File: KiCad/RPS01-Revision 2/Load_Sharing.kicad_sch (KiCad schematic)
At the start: 11 parts, among them U1 NP100P04PLG-E1-AY, U2 NP100P04PLG-E1-AY, U3 NP100P04PLG-E1-AY, U4 LTC4416EMS-1-TRPBF, U5 NP100P04PLG-E1-AY, U6 NP100P04PLG-E1-AY, U7 NP100P04PLG-E1-AY

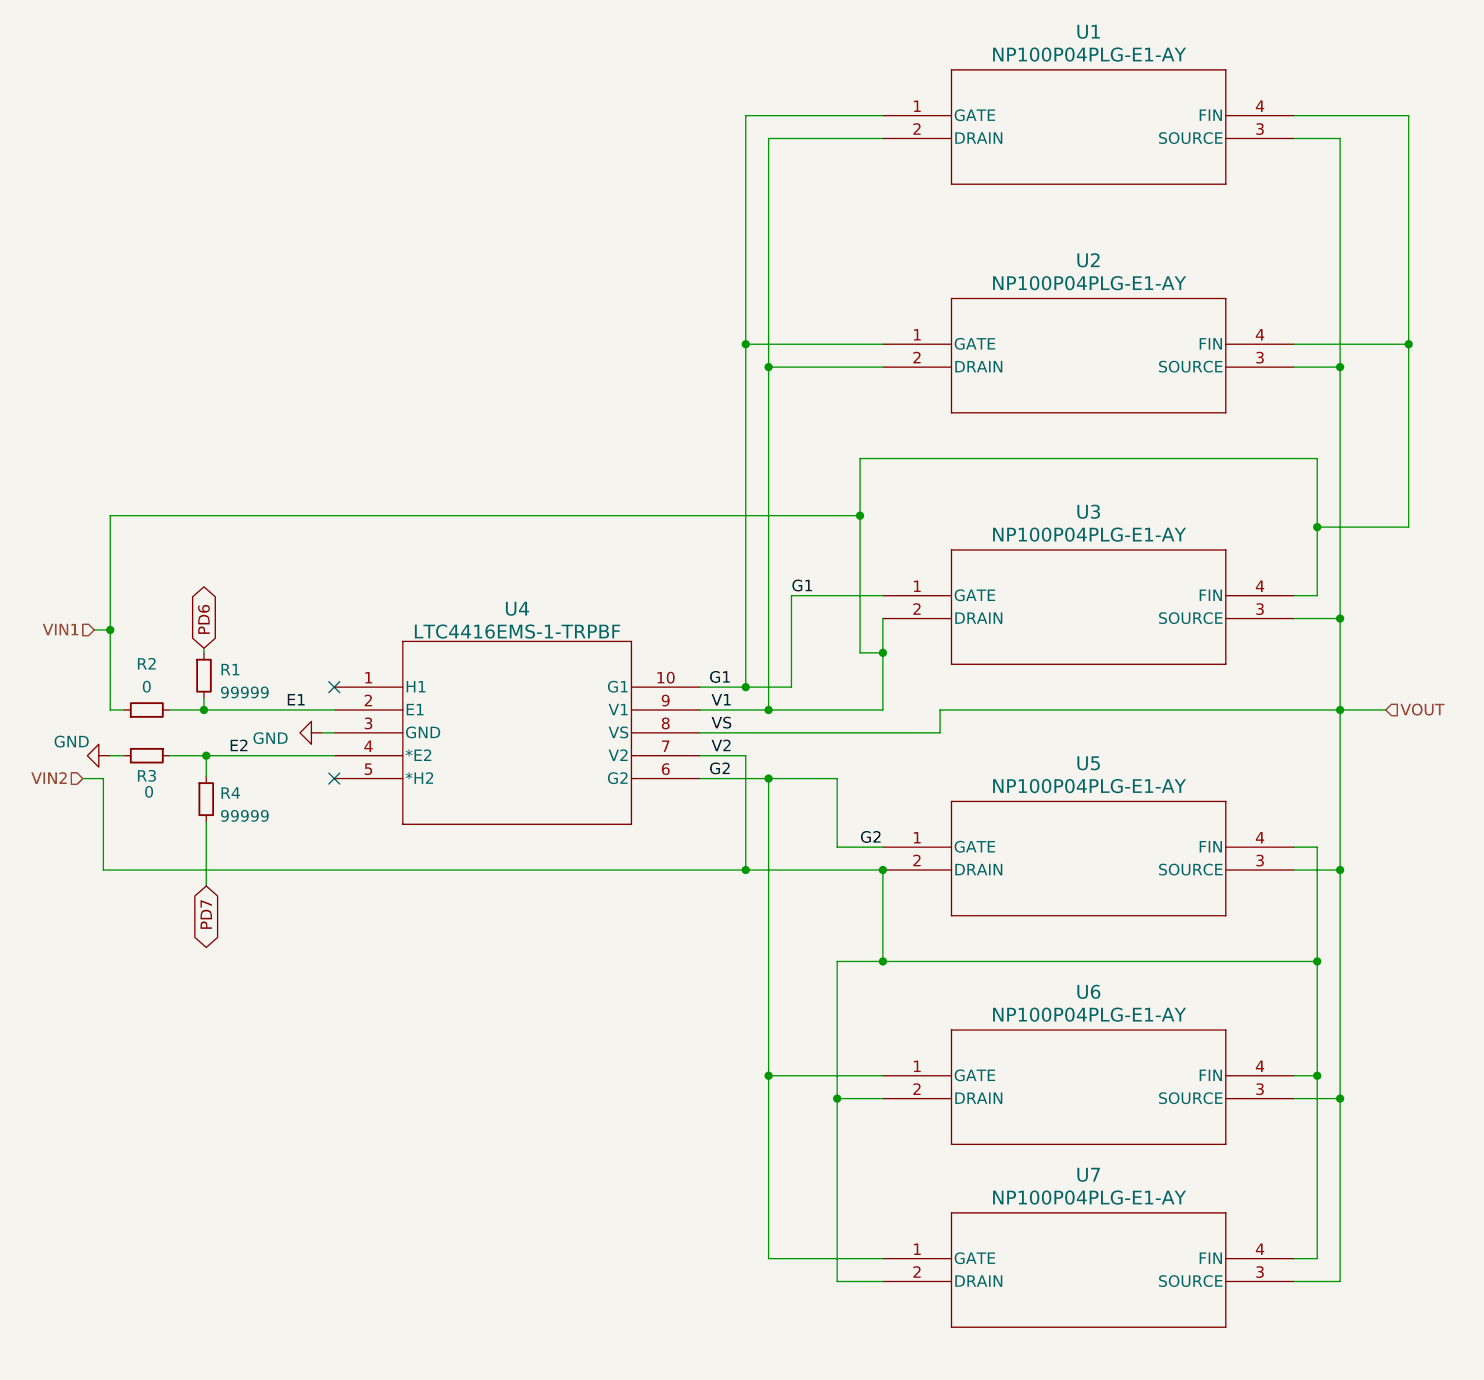
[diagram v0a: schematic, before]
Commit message: Load Sharing
Changed wiring for the reversed MOSFETs
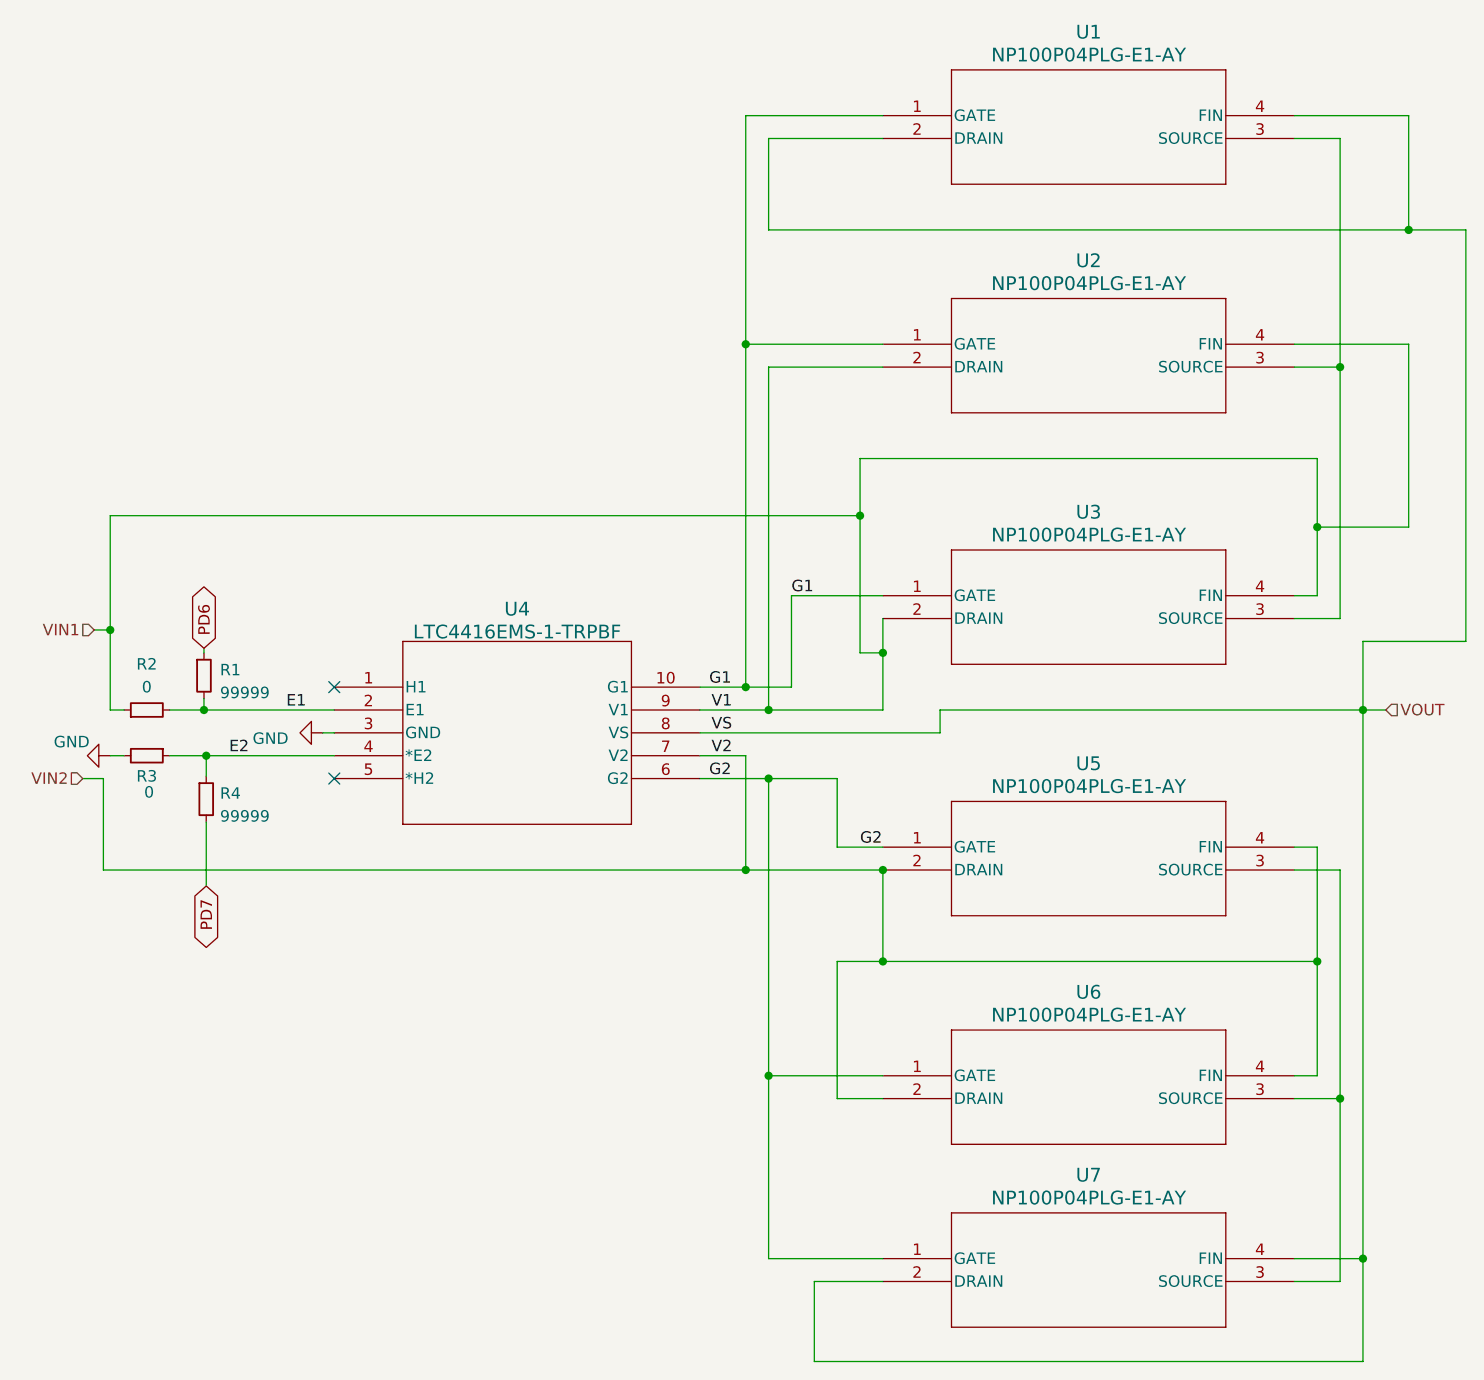
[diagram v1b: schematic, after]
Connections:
- net VIN1: no longer U1.2 (DRAIN), U1.4 (FIN)
- net VIN2: no longer U7.2 (DRAIN), U7.4 (FIN)
- net VOUT: now also U1.2 (DRAIN), U1.4 (FIN), U7.2 (DRAIN), U7.4 (FIN); no longer U1.3 (SOURCE), U2.3 (SOURCE), U3.3 (SOURCE), U5.3 (SOURCE), U6.3 (SOURCE), U7.3 (SOURCE)
- new net: U1.3 (SOURCE), U2.3 (SOURCE), U3.3 (SOURCE)
- new net: U5.3 (SOURCE), U6.3 (SOURCE), U7.3 (SOURCE)
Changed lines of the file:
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@@
 (kicad_sch (version 20230121) (generator eeschema)
   (paper "A4")
-  (junction (at 162.56 104.14) (diameter 0) (color 0 0 0 0)
-  )
-  (junction (at 162.56 93.98) (diameter 0) (color 0 0 0 0)
-  )
-  (junction (at 160.02 144.78) (diameter 0) (color 0 0 0 0)
+  (junction (at 165.1 165.1) (diameter 0) (color 0 0 0 0)
   )
   (junction (at 111.76 121.92) (diameter 0) (color 0 0 0 0)
@@
   (junction (at 162.56 66.04) (diameter 0) (color 0 0 0 0)
   )
-  (junction (at 162.56 121.92) (diameter 0) (color 0 0 0 0)
-  )
   (junction (at 36.576 109.22) (diameter 0) (color 0 0 0 0)
   )
@@
   (junction (at 96.52 121.92) (diameter 0) (color 0 0 0 0)
   )
+  (junction (at 165.1 104.14) (diameter 0) (color 0 0 0 0)
+  )
   (junction (at 99.06 111.76) (diameter 0) (color 0 0 0 0)
   )
   (junction (at 160.02 132.08) (diameter 0) (color 0 0 0 0)
   )
-  (junction (at 170.18 63.5) (diameter 0) (color 0 0 0 0)
-  )
-  (junction (at 106.68 147.32) (diameter 0) (color 0 0 0 0)
-  )
   (junction (at 111.76 132.08) (diameter 0) (color 0 0 0 0)
   )
@@
   (junction (at 111.76 97.79) (diameter 0) (color 0 0 0 0)
   )
-  (junction (at 99.06 66.04) (diameter 0) (color 0 0 0 0)
-  )
   (junction (at 99.06 104.14) (diameter 0) (color 0 0 0 0)
   )
@@
   )
   (junction (at 36.322 104.14) (diameter 0) (color 0 0 0 0)
+  )
+  (junction (at 170.18 50.8) (diameter 0) (color 0 0 0 0)
   )
   (no_connect (at 50.8 111.76))
@@
     (stroke (width 0) (type default))
   )
+  (wire (pts (xy 176.53 50.8) (xy 176.53 96.52))
+    (stroke (width 0) (type default))
+  )
+  (wire (pts (xy 165.1 96.52) (xy 165.1 104.14))
+    (stroke (width 0) (type default))
+  )
   (wire (pts (xy 106.68 132.08) (xy 111.76 132.08))
     (stroke (width 0) (type default))
@@
     (stroke (width 0) (type default))
   )
+  (wire (pts (xy 170.18 38.1) (xy 170.18 50.8))
+    (stroke (width 0) (type default))
+  )
   (wire (pts (xy 99.06 104.14) (xy 111.76 104.14))
     (stroke (width 0) (type default))
@@
     (stroke (width 0) (type default))
   )
-  (wire (pts (xy 106.68 167.64) (xy 111.76 167.64))
-    (stroke (width 0) (type default))
-  )
   (wire (pts (xy 99.06 144.78) (xy 99.06 165.1))
     (stroke (width 0) (type default))
@@
     (stroke (width 0) (type default))
   )
+  (wire (pts (xy 157.48 165.1) (xy 165.1 165.1))
+    (stroke (width 0) (type default))
+  )
   (wire (pts (xy 157.48 66.04) (xy 162.56 66.04))
     (stroke (width 0) (type default))
@@
     (stroke (width 0) (type default))
   )
-  (wire (pts (xy 162.56 104.14) (xy 162.56 121.92))
-    (stroke (width 0) (type default))
-  )
-  (wire (pts (xy 106.68 147.32) (xy 106.68 167.64))
-    (stroke (width 0) (type default))
-  )
-  (wire (pts (xy 162.56 104.14) (xy 162.56 93.98))
+  (wire (pts (xy 104.14 176.53) (xy 165.1 176.53))
     (stroke (width 0) (type default))
   )
@@
     (stroke (width 0) (type default))
   )
+  (wire (pts (xy 165.1 176.53) (xy 165.1 165.1))
+    (stroke (width 0) (type default))
+  )
   (wire (pts (xy 32.512 104.14) (xy 36.322 104.14))
     (stroke (width 0) (type default))
@@
     (stroke (width 0) (type default))
   )
-  (wire (pts (xy 160.02 165.1) (xy 157.48 165.1))
+  (wire (pts (xy 111.76 167.64) (xy 104.14 167.64))
+    (stroke (width 0) (type default))
+  )
+  (wire (pts (xy 165.1 104.14) (xy 167.64 104.14))
     (stroke (width 0) (type default))
   )
@@
     (stroke (width 0) (type default))
   )
+  (wire (pts (xy 99.06 50.8) (xy 170.18 50.8))
+    (stroke (width 0) (type default))
+  )
   (wire (pts (xy 96.52 63.5) (xy 96.52 38.1))
     (stroke (width 0) (type default))
@@
     (stroke (width 0) (type default))
   )
+  (wire (pts (xy 170.18 50.8) (xy 176.53 50.8))
+    (stroke (width 0) (type default))
+  )
   (wire (pts (xy 160.02 144.78) (xy 160.02 132.08))
     (stroke (width 0) (type default))
   )
-  (wire (pts (xy 99.06 66.04) (xy 99.06 40.64))
-    (stroke (width 0) (type default))
-  )
   (wire (pts (xy 25.908 95.25) (xy 25.908 104.14))
     (stroke (width 0) (type default))
@@
     (stroke (width 0) (type default))
   )
+  (wire (pts (xy 165.1 165.1) (xy 165.1 104.14))
+    (stroke (width 0) (type default))
+  )
   (wire (pts (xy 160.02 76.2) (xy 160.02 83.82))
     (stroke (width 0) (type default))
@@
     (stroke (width 0) (type default))
   )
+  (wire (pts (xy 104.14 167.64) (xy 104.14 176.53))
+    (stroke (width 0) (type default))
+  )
   (wire (pts (xy 160.02 119.38) (xy 160.02 132.08))
     (stroke (width 0) (type default))
@@
     (stroke (width 0) (type default))
   )
-  (wire (pts (xy 162.56 104.14) (xy 167.64 104.14))
+  (wire (pts (xy 118.11 104.14) (xy 165.1 104.14))
     (stroke (width 0) (type default))
   )
@@
     (stroke (width 0) (type default))
   )
-  (wire (pts (xy 118.11 104.14) (xy 162.56 104.14))
-    (stroke (width 0) (type default))
-  )
   (wire (pts (xy 157.48 38.1) (xy 170.18 38.1))
     (stroke (width 0) (type default))
   )
-  (wire (pts (xy 160.02 144.78) (xy 160.02 165.1))
-    (stroke (width 0) (type default))
-  )
   (wire (pts (xy 162.56 121.92) (xy 157.48 121.92))
     (stroke (width 0) (type default))
@@
     (stroke (width 0) (type default))
   )
-  (wire (pts (xy 170.18 38.1) (xy 170.18 63.5))
+  (wire (pts (xy 99.06 40.64) (xy 99.06 50.8))
     (stroke (width 0) (type default))
   )
@@
     (stroke (width 0) (type default))
   )
+  (wire (pts (xy 176.53 96.52) (xy 165.1 96.52))
+    (stroke (width 0) (type default))
+  )
